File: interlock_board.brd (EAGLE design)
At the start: 49.5 x 73.7 mm, 6 parts, among them X1 1-227161-0

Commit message: Update interlock_board.brd
Moved various wires so they are not as close to the various pins on the board.
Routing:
- net N$2: track 29.6 -> 28.1 mm
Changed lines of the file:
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@@
 <contactref element="U$1" pad="J1.3"/>
 <wire x1="35.56" y1="30.48" x2="35.56" y2="29.24326875" width="0.2032" layer="1"/>
-<wire x1="35.56" y1="29.24326875" x2="37.0076" y2="27.79566875" width="0.2032" layer="1"/>
-<wire x1="37.0076" y1="10.16" x2="45.72" y2="10.16" width="0.2032" layer="1"/>
-<wire x1="37.0076" y1="27.79566875" x2="37.0076" y2="10.16" width="0.2032" layer="1"/>
+<wire x1="35.56" y1="29.24326875" x2="39.5476" y2="25.25566875" width="0.2032" layer="1"/>
+<wire x1="39.5476" y1="10.16" x2="45.72" y2="10.16" width="0.2032" layer="1"/>
+<wire x1="39.5476" y1="25.25566875" x2="39.5476" y2="10.16" width="0.2032" layer="1"/>
 </signal>
 <signal name="N$4">
@@
 <signal name="N$1">
 <contactref element="JP1" pad="2"/>
-<wire x1="35.56" y1="8.7296" x2="34.4504" y2="8.7296" width="0.2032" layer="1"/>
-<wire x1="34.4504" y1="8.7296" x2="34.4504" y2="7.62" width="0.2032" layer="1"/>
-<wire x1="34.4504" y1="7.62" x2="20.32" y2="7.62" width="0.2032" layer="1"/>
-<wire x1="14.8176" y1="7.62" x2="14.8176" y2="8.49714375" width="0.2032" layer="1"/>
-<wire x1="14.8176" y1="8.49714375" x2="13.57714375" y2="9.7376" width="0.2032" layer="1"/>
-<wire x1="13.57714375" y1="9.7376" x2="12.7" y2="9.7376" width="0.2032" layer="1"/>
-<wire x1="12.7" y1="9.7376" x2="12.7" y2="16.51" width="0.2032" layer="1"/>
+<wire x1="31.75" y1="9.9996" x2="29.21" y2="9.9996" width="0.2032" layer="1"/>
+<wire x1="29.21" y1="9.9996" x2="22.6996" y2="9.9996" width="0.2032" layer="1"/>
+<wire x1="22.6996" y1="9.9996" x2="20.32" y2="7.62" width="0.2032" layer="1"/>
+<wire x1="16.0876" y1="7.62" x2="16.0876" y2="16.51" width="0.2032" layer="1"/>
 <wire x1="12.7" y1="16.51" x2="12.7" y2="24.09673125" width="0.2032" layer="1"/>
 <wire x1="12.7" y1="24.09673125" x2="11.2524" y2="25.54433125" width="0.2032" layer="1"/>
 <wire x1="11.2524" y1="25.54433125" x2="11.2524" y2="27.79566875" width="0.2032" layer="1"/>
 <wire x1="11.2524" y1="27.79566875" x2="12.7" y2="29.24326875" width="0.2032" layer="1"/>
-<wire x1="20.32" y1="7.62" x2="14.8176" y2="7.62" width="0.2032" layer="1"/>
+<wire x1="20.32" y1="7.62" x2="16.0876" y2="7.62" width="0.2032" layer="1"/>
 <contactref element="U$1" pad="J2.3"/>
 <contactref element="PAD1" pad="1"/>
 <contactref element="U$2" pad="VIN"/>
-<wire x1="20.32" y1="16.51" x2="12.7" y2="16.51" width="0.2032" layer="1"/>
-<wire x1="35.56" y1="8.7296" x2="35.56" y2="10.16" width="0" layer="19" extent="1-1"/>
-<wire x1="12.7" y1="30.48" x2="12.7" y2="29.24326875" width="0" layer="19" extent="1-1"/>
+<wire x1="20.32" y1="16.51" x2="16.0876" y2="16.51" width="0.2032" layer="1"/>
+<wire x1="35.56" y1="10.16" x2="29.3704" y2="10.16" width="0.1524" layer="1"/>
+<wire x1="29.3704" y1="10.16" x2="29.21" y2="9.9996" width="0.1524" layer="1"/>
+<wire x1="16.0876" y1="16.51" x2="12.7" y2="16.51" width="0.1524" layer="1"/>
+<wire x1="12.7" y1="29.24326875" x2="12.7" y2="30.48" width="0" layer="19" extent="1-1"/>
 </signal>
 </signals>

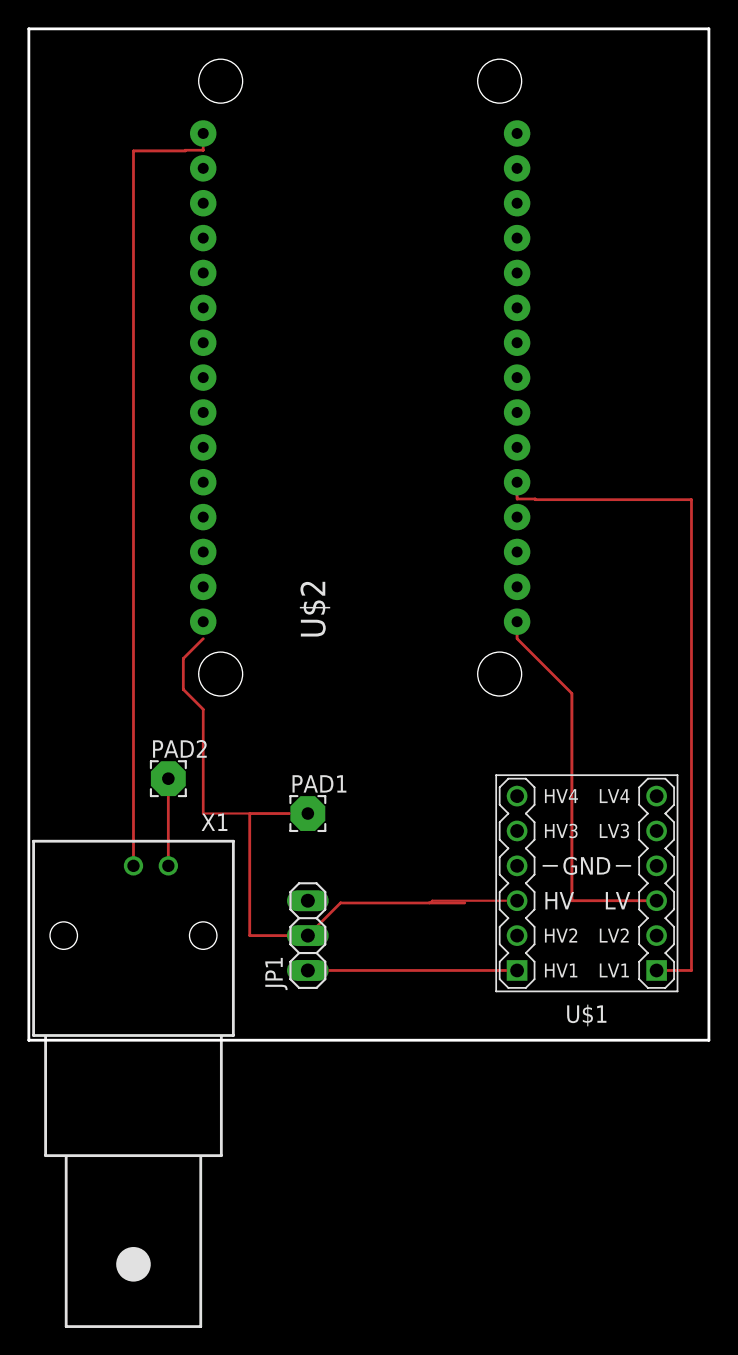
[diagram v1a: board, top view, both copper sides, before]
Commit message: Update with Alessandro's help
This update increases the copper trace size from 0.008" to 0.024" and moves them to the bottom layer, uses an updated BNC connector footprint (from JQI library) for better mechanical stability, and increased some hole sizes from 800 micron to 0.04".
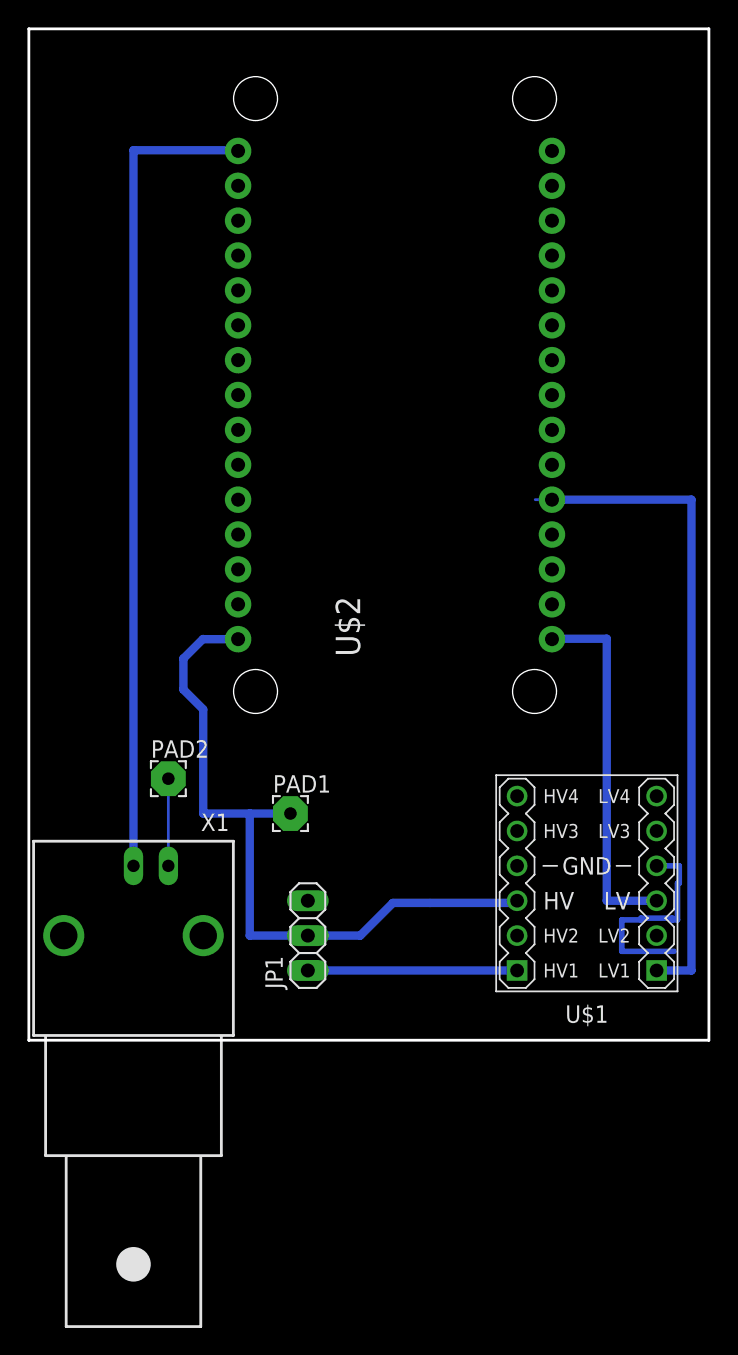
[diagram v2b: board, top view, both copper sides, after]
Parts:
- U$2: device ESP12E_DEVKIT:ESP12E_DEVKIT -> interlock_board:ESP12E_DEVKIT
- X1: value 1-227161-0 -> BNC-H; device con-coax:AMP_227161 -> connector-jqi:BNC90
- moved U$2 2.84 mm to (26.7, 47.0)
- moved PAD1 1.27 mm to (19.1, 16.5)
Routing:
- net GND: track 6.35 -> 22.5 mm
- net N$3: track 50.8 -> 48.2 mm
- net N$2: track 28.1 -> 26.7 mm
- net N$4: track 58.4 -> 59.8 mm
- net N$1: track 53.5 -> 52.4 mm
- added copper zone on layer 16, net GND
- removed copper zone on layer 1, net GND
